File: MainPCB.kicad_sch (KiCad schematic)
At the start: 81 parts, among them IC1 VNH7070ASTR, IC2 VNH7070ASTR, IC3 VNH7070ASTR, IC4 VNH7070ASTR, IC5 VNH7070ASTR, J1 Conn_01x06, J10 Conn_01x02, J101 TYPEC-305-ACP16H458, J11 Conn_01x03, J12 Conn_01x03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

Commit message: Finished Power Wiring and Fixed Schematic Bus Issues
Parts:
- removed J12, J6: Conn_01x03, Connector_JST:JST_XH_B3B-XH-A_1x03_P2.50mm_Vertical, symbol Connector_Generic:Conn_01x03
- removed J7: Conn_01x02, Connector_JST:JST_XH_B2B-XH-A_1x02_P2.50mm_Vertical, symbol Connector_Generic:Conn_01x02
- added J2: Conn_01x05_Pin, Connector_JST:JST_XH_B5B-XH-A_1x05_P2.50mm_Vertical, symbol Connector:Conn_01x05_Pin
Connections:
- net 12V: now also J2.1 (Pin_1)
- net 3.3V: now also J2.3 (Pin_3)
- net 48V: now also J2.5 (Pin_5)
- net 5V: now also J2.2 (Pin_2)
- net GND: now also J2.4 (Pin_4)

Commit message: Did a bunch of routing, freerouting is broken, and im lowk tired
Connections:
- net DIR4A: no longer R3.1
- net DIR4B: no longer R4.1
- net PWM4: no longer R5.2
- net PWM5: now also R5.2
- net ESC_PWM: no longer names the net of U12.3 (1_TX1_CTX2_MISO1)
- net LEDPulse: no longer names the net of U12.2 (0_RX1_CRX2_CS1)
- new net DIR5A: R3.1
- new net DIR5B: R4.1

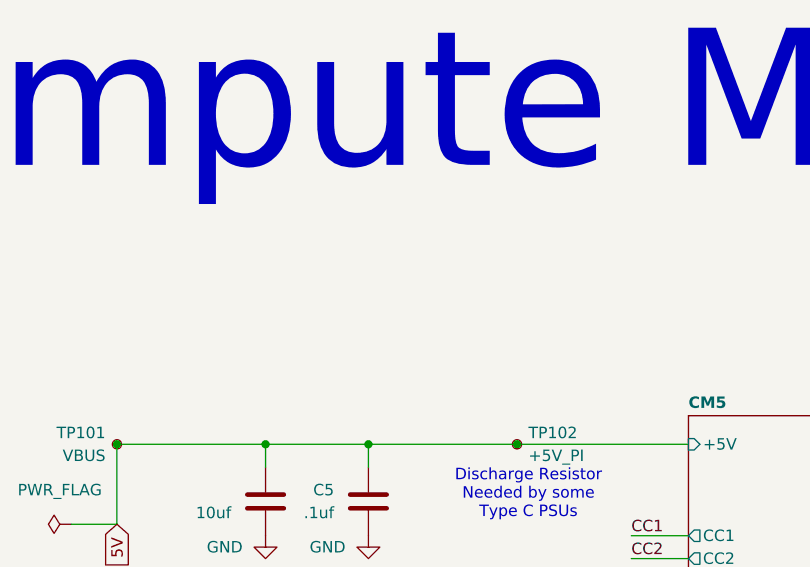
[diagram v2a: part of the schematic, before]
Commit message: Finished Routing
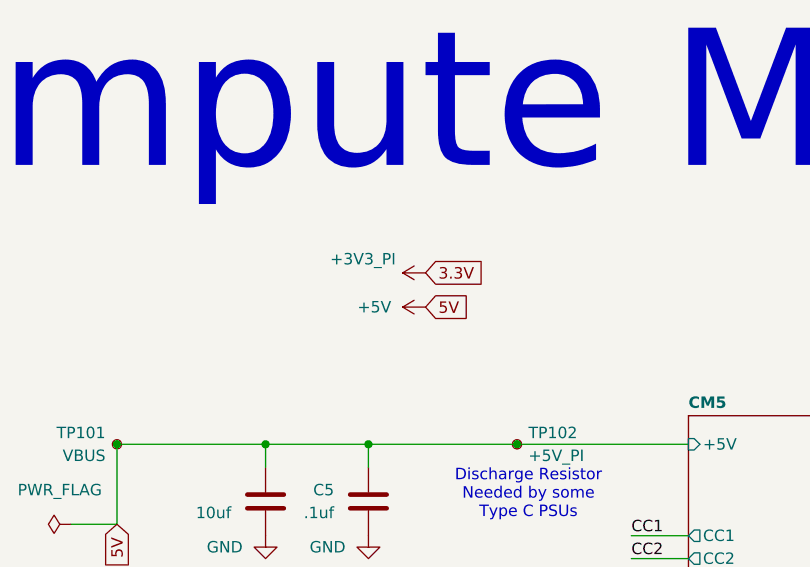
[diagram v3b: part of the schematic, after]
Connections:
- net 3.3V is gone; now on net +3V3_PI: C3.1, C4.1, C7.1, C8.1, J10.1 (Pin_1), J11.1 (Pin_1), J2.3 (Pin_3), J3.12 (Pin_12), JP1.2 (B), U4.5 (VIN)
- net 5V renamed +5V
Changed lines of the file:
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@@
 		)
 	)
+	(global_label "5V"
+		(shape input)
+		(at 566.42 52.07 0)
+		(fields_autoplaced yes)
+		(effects
+			(font
+				(size 1.27 1.27)
+			)
+			(justify left)
+		)
+		(property "Intersheetrefs" "${INTERSHEET_REFS}"
+			(at 571.7033 52.07 0)
+			(effects
+				(font
+					(size 1.27 1.27)
+				)
+				(justify left)
+				(hide yes)
+			)
+		)
+	)
 	(global_label "PWM2"
 		(shape input)
@@
 		)
 	)
+	(global_label "3.3V"
+		(shape input)
+		(at 566.42 48.26 0)
+		(fields_autoplaced yes)
+		(effects
+			(font
+				(size 1.27 1.27)
+			)
+			(justify left)
+		)
+		(property "Intersheetrefs" "${INTERSHEET_REFS}"
+			(at 573.5176 48.26 0)
+			(effects
+				(font
+					(size 1.27 1.27)
+				)
+				(justify left)
+				(hide yes)
+			)
+		)
+	)
 	(global_label "DIR1A"
 		(shape input)
@@
 	)
 	(symbol
+		(lib_id "power:+3V3")
+		(at 566.42 48.26 90)
+		(unit 1)
+		(exclude_from_sim no)
+		(in_bom yes)
+		(on_board yes)
+		(dnp no)
+		(property "Reference" "#PWR013"
+			(at 570.23 48.26 0)
+			(effects
+				(font
+					(size 1.27 1.27)
+				)
+				(hide yes)
+			)
+		)
+		(property "Value" "+3V3_PI"
+			(at 563.118 46.736 90)
+			(effects
+				(font
+					(size 1.27 1.27)
+				)
+				(justify left)
+			)
+		)
+		(property "Footprint" ""
+			(at 566.42 48.26 0)
+			(effects
+				(font
+					(size 1.27 1.27)
+				)
+				(hide yes)
+			)
+		)
+		(property "Datasheet" ""
+			(at 566.42 48.26 0)
+			(effects
+				(font
+					(size 1.27 1.27)
+				)
+				(hide yes)
+			)
+		)
+		(property "Description" "Power symbol creates a global label with name \"+3V3\""
+			(at 566.42 48.26 0)
+			(effects
+				(font
+					(size 1.27 1.27)
+				)
+				(hide yes)
+			)
+		)
+		(pin "1"
+		)
+		(instances
+			(project "MainPCB"
+				(path "/42b49b64-9684-402a-8d6b-7bff18ed389a"
+					(reference "#PWR013")
+					(unit 1)
+				)
+			)
+		)
+	)
+	(symbol
 		(lib_id "Connector_Generic:Conn_01x02")
 		(at 109.22 31.75 180)
@@
 					(unit 1)
 				)
+			)
+		)
+	)
+	(symbol
+		(lib_id "power:+5V")
+		(at 566.42 52.07 90)
+		(unit 1)
+		(exclude_from_sim no)
+		(in_bom yes)
+		(on_board yes)
+		(dnp no)
+		(fields_autoplaced yes)
+		(property "Reference" "#PWR014"
+			(at 570.23 52.07 0)
+			(effects
+				(font
+					(size 1.27 1.27)
+				)
+				(hide yes)
+			)
+		)
+		(property "Value" "+5V"
+			(at 562.61 52.0699 90)
+			(effects
+				(font
+					(size 1.27 1.27)
+				)
+				(justify left)
+			)
+		)
+		(property "Footprint" ""
+			(at 566.42 52.07 0)
+			(effects
+				(font
+					(size 1.27 1.27)
+				)
+				(hide yes)
+			)
+		)
+		(property "Datasheet" ""
+			(at 566.42 52.07 0)
+			(effects
+				(font
+					(size 1.27 1.27)
+				)
+				(hide yes)
+			)
+		)
+		(property "Description" "Power symbol creates a global label with name \"+5V\""
+			(at 566.42 52.07 0)
+			(effects
+				(font
+					(size 1.27 1.27)
+				)
+				(hide yes)
+			)
+		)
+		(pin "1"
+		)
+		(instances
+			(project "MainPCB"
+				(path "/42b49b64-9684-402a-8d6b-7bff18ed389a"
+					(reference "#PWR014")
+					(unit 1)
+				)

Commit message: Added LiDAR and LCD connections
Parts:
- removed TP104, TP105, TP106: GND, TestPoint:TestPoint_THTPad_D1.0mm_Drill0.5mm, symbol Connector:TestPoint_Small
- added J6, J7: Conn_01x04_Pin, Connector_JST:JST_XH_B4B-XH-A_1x04_P2.50mm_Vertical, symbol Connector:Conn_01x04_Pin
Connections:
- net +5V: now also J6.1 (Pin_1), J7.1 (Pin_1)
- net CS6: now also U12.25 (33_MCLK2); no longer U12.27 (35_TX8)
- net GND: now also J6.2 (Pin_2), J7.2 (Pin_2)
- net RX8 -> TX: now reaches U12.26 (34_RX8)
- net RX8 -> TX: now also J7.4 (Pin_4)
- new net PWM-LIDAR: J6.3 (Pin_3)
- new net RX->TX - LIDAR: J6.4 (Pin_4)
- new net TX8 -> RX: J7.3 (Pin_3), U12.27 (35_TX8)
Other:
- sheet CM5 ports: added GPIO12, GPIO13; removed none

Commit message: Added Changed for Line and Kicker PCB
Still need to work out boost converter position
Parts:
- removed C3: 10uf, Capacitor_SMD:C_0805_2012Metric, symbol Device:C
- removed C4: .1uf, Capacitor_SMD:C_0805_2012Metric, symbol Device:C
- removed J2: Conn_01x05_Pin, Connector_JST:JST_XH_B5B-XH-A_1x05_P2.50mm_Vertical, symbol Connector:Conn_01x05_Pin
- removed J3: Conn_01x12, Connector_IDC:IDC-Header_2x06_P2.54mm_Vertical, symbol Connector_Generic:Conn_01x12
- removed J9: Conn_01x02, Connector_JST:JST_XH_B2B-XH-A_1x02_P2.50mm_Vertical, symbol Connector_Generic:Conn_01x02
- removed R18: 10k, Capacitor_SMD:C_0805_2012Metric_Pad1.18x1.45mm_HandSolder, symbol Device:R
- removed SW6: SW_DPST_x2, SlideSW:SPDT_OS102011_CNK, symbol Switch:SW_DPST_x2
- removed U3: BoostConverter, BoostConverter:Boost_Convertor_LM2577, symbol BoostConverter:BoostConverter
- removed U6: N channel, Package_TO_SOT_THT:TO-220-3_Vertical, symbol Transistor_FET:2N7002K
- added J2: Conn_01x04_Pin, Connector_JST:JST_XH_B4B-XH-A_1x04_P2.50mm_Vertical, symbol Connector:Conn_01x04_Pin
- added J9: Conn_01x06_Pin, Connector_JST:JST_XH_B6B-XH-A_1x06_P2.50mm_Vertical, symbol Connector:Conn_01x06_Pin
- added U21: V_Regulator3.3v, Custom:Pololu5V3.4A, symbol Voltage Regulator:V_Regulator_-_5v
- added U22: V_Regulator5v, Custom:Pololu5V3.4A, symbol Voltage Regulator:V_Regulator_-_5v
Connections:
- net MISO is gone; now on net DIR5B: U12.14 (12_MISO_MQSL)
- net MOSI is gone; now on net DIR5A: U12.13 (11_MOSI_CTX1)
- net +3V3_PI: now also J9.3 (Pin_3), U21.5 (OUT+)
- net +5V: now also J9.1 (Pin_1), U22.5 (OUT+)
- net 12V: now also J2.2 (Pin_2), J9.4 (Pin_4), U21.3 (IN+), U22.3 (IN+)
- net 48V: now also J2.3 (Pin_3)
- net GND: now also J2.4 (Pin_4), J9.2 (Pin_2), U21.4 (OUT-), U22.4 (OUT-)
- net Kicker: now also J2.1 (Pin_1)
- net CS1 renamed RX(4.1)-TX(4.0)
- net RX(4.1)-TX(4.0): now also J9.5 (Pin_5)
- net CS2 renamed TX(4.1)-RX(4.0)
- net TX(4.1)-RX(4.0): now also J9.6 (Pin_6)
- net CS3: no longer names the net of U12.38 (16_A2_RX4_SCL1)
- net CS4: no longer names the net of U12.29 (37_CS)
- net CS5: no longer names the net of U12.28 (36_CS)
- net CS6: no longer names the net of U12.25 (33_MCLK2)
- net SCK1: no longer names the net of U12.35 (13_SCK_LED)

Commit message: Made Changes
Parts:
- removed J2: Conn_01x04_Pin, Connector_JST:JST_XH_B4B-XH-A_1x04_P2.50mm_Vertical, symbol Connector:Conn_01x04_Pin
- added J3: Conn_01x03_Pin, Connector_JST:JST_XH_B3B-XH-A_1x03_P2.50mm_Vertical, symbol Connector:Conn_01x03_Pin
- R1, R10, R11, R12, R13, R14, R15, R16, R17, R3, R4, R5, R7, R8, R9: value 100 -> 1k
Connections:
- net 12V: now also J3.2 (Pin_2)
- net GND: now also J3.3 (Pin_3)
- net Kicker: now also J3.1 (Pin_1)
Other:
- note removed: "Boost Converter"

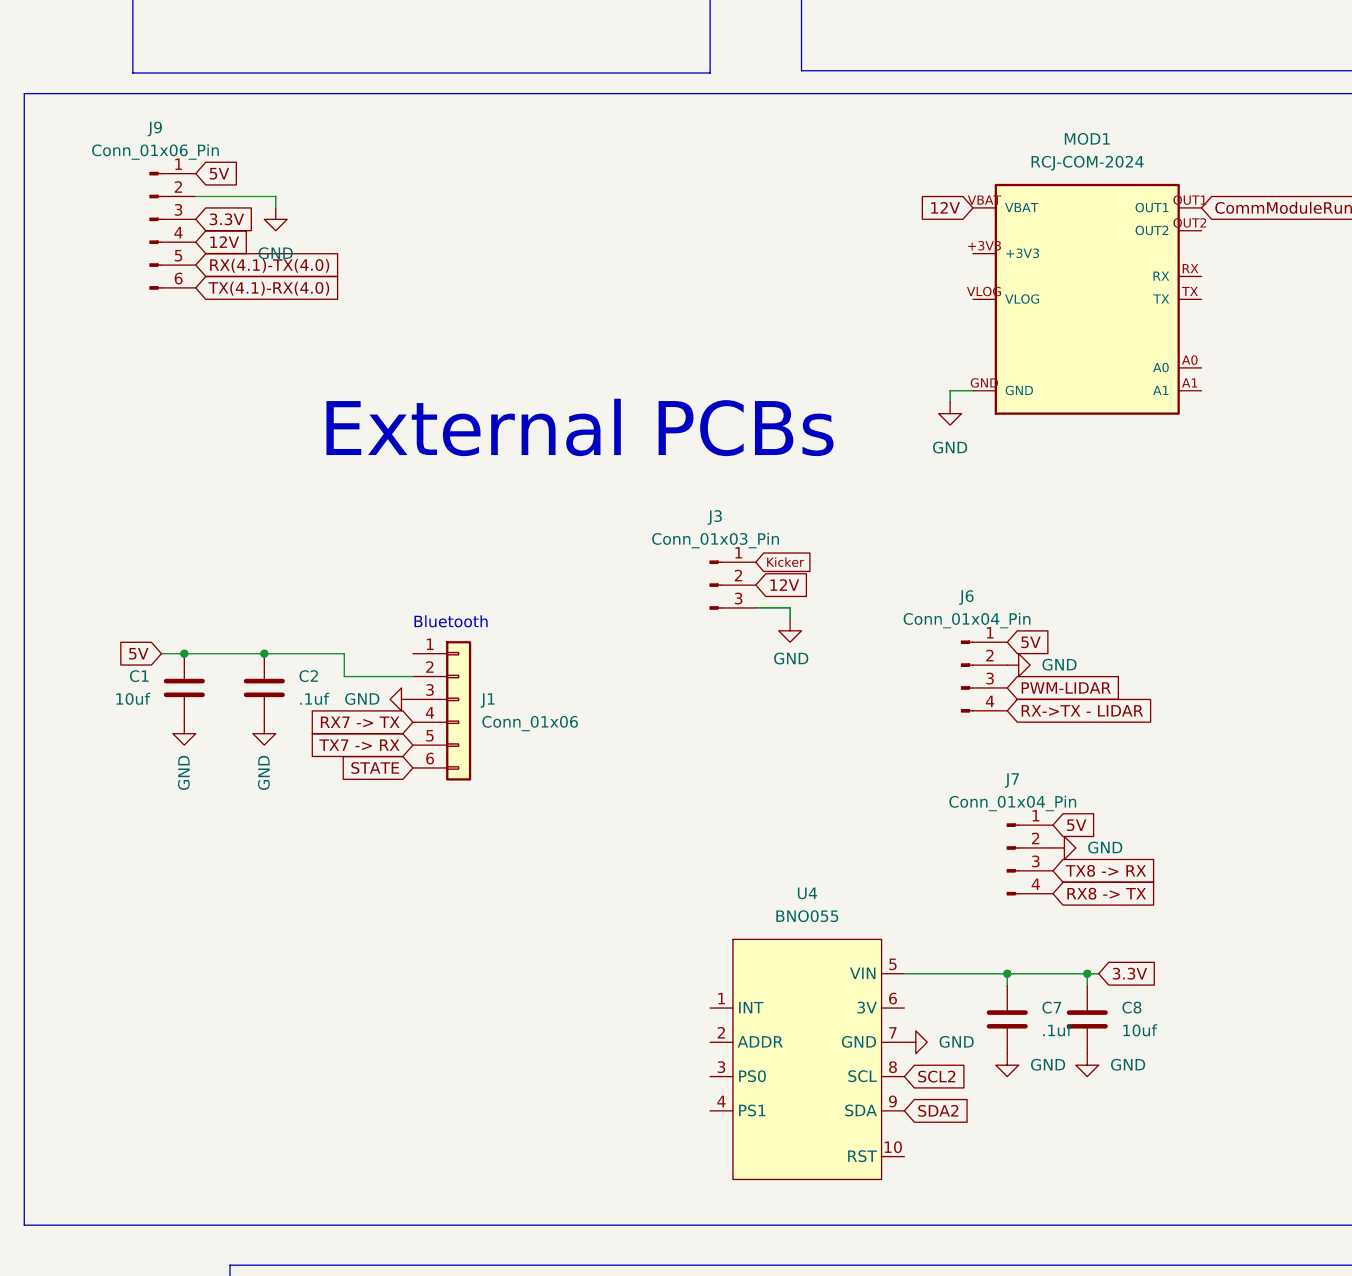
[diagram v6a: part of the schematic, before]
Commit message: Added Voltage Dividers for UNO
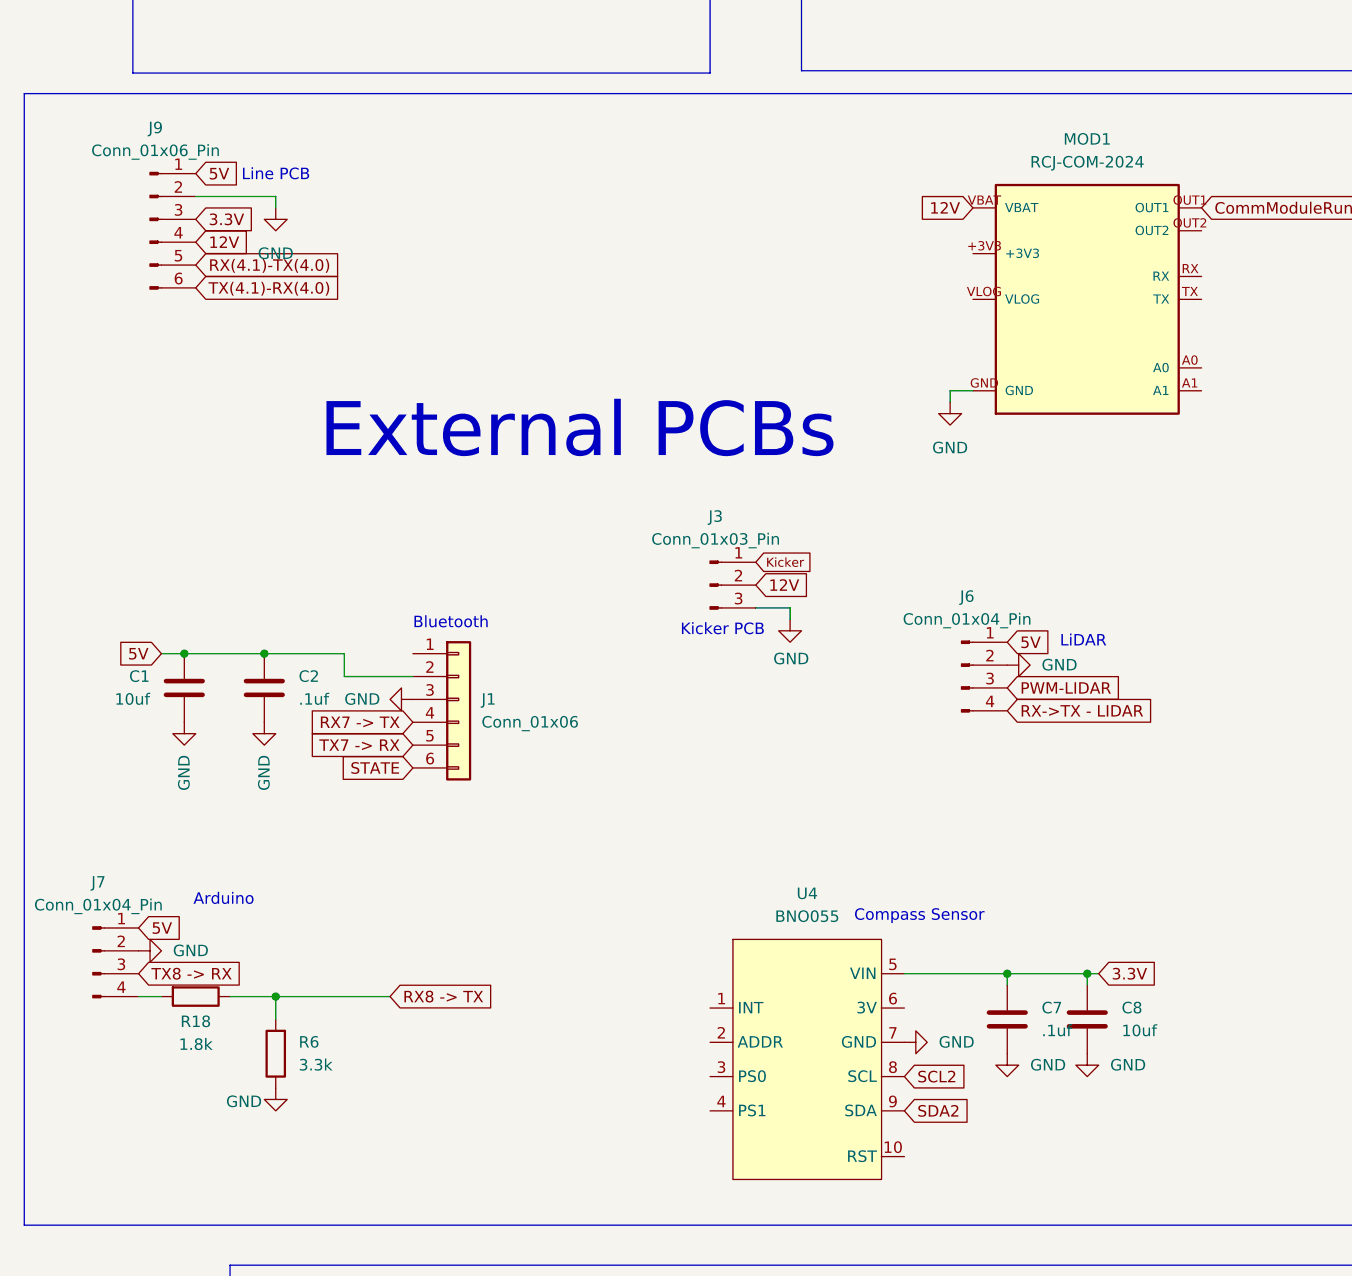
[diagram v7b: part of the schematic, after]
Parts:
- added R18: 1.8k, Resistor_SMD:R_0805_2012Metric_Pad1.20x1.40mm_HandSolder, symbol Device:R
- added R6: 3.3k, Resistor_SMD:R_0805_2012Metric_Pad1.20x1.40mm_HandSolder, symbol Device:R
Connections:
- net GND: now also R6.1
- net RX8 -> TX: now also R18.1, R6.2; no longer J7.4 (Pin_4)
- new net: J7.4 (Pin_4), R18.2
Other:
- note added: "Arduino"
- note added: "Compass Sensor"
- note added: "Kicker PCB"
- note added: "LiDAR"
- note added: "Line PCB"
- moved on the sheet: J7

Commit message: Not sending 12V to Line
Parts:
- removed TP101: VBUS, TestPoint:TestPoint_Pad_D1.0mm, symbol Connector:TestPoint_Small
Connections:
- net 12V: no longer J9.4 (Pin_4)
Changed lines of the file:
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@@
 	)
 	(junction
-		(at 532.13 67.31)
-		(diameter 0)
-		(color 0 0 0 0)
-	)
-	(junction
 		(at 270.51 368.3)
 		(diameter 0)
@@
 		)
 	)
-	(global_label "12V"
-		(shape input)
-		(at 35.56 175.26 0)
-		(fields_autoplaced yes)
-		(effects
-			(font
-				(size 1.27 1.27)
-			)
-			(justify left)
-		)
-		(property "Intersheetrefs" "${INTERSHEET_REFS}"
-			(at 42.0528 175.26 0)
-			(hide yes)
-			(show_name no)
-			(do_not_autoplace no)
-			(effects
-				(font
-					(size 1.27 1.27)
-				)
-				(justify left)
-			)
-		)
-	)
 	(global_label "PWM4"
 		(shape input)
@@
 					(unit 1)
 				)
-			)
-		)
-	)
-	(symbol
-		(lib_id "Connector:TestPoint_Small")
-		(at 532.13 67.31 0)
-		(mirror y)
-		(unit 1)
-		(body_style 1)
-		(exclude_from_sim no)
-		(in_bom no)
-		(on_board yes)
-		(in_pos_files yes)
-		(dnp no)
-		(property "Reference" "TP101"
-			(at 530.86 66.0399 0)
-			(show_name no)
-			(do_not_autoplace no)
-			(effects
-				(font
-					(size 1.27 1.27)
-				)
-				(justify left)
-			)
-		)
-		(property "Value" "VBUS"
-			(at 530.86 68.5799 0)
-			(show_name no)
-			(do_not_autoplace no)
-			(effects
-				(font
-					(size 1.27 1.27)
-				)
-				(justify left)
-			)
-		)
-		(property "Footprint" "TestPoint:TestPoint_Pad_D1.0mm"
-			(at 527.05 67.31 0)
-			(hide yes)
-			(show_name no)
-			(do_not_autoplace no)
-			(effects
-				(font
-					(size 1.27 1.27)
-				)
-			)
-		)
-		(property "Datasheet" ""
-			(at 527.05 67.31 0)
-			(hide yes)
-			(show_name no)
-			(do_not_autoplace no)
-			(effects
-				(font
-					(size 1.27 1.27)
-				)
-			)
-		)
-		(property "Description" "test point"
-			(at 532.13 67.31 0)
-			(hide yes)
-			(show_name no)
-			(do_not_autoplace no)
-			(effects
-				(font
-					(size 1.27 1.27)
-				)
-			)
-		)
-		(pin "1"
-		)
-		(instances
-			(project "MainPCB"
-				(path "/42b49b64-9684-402a-8d6b-7bff18ed389a"
-					(reference "TP101")
-					(unit 1)
-				)
